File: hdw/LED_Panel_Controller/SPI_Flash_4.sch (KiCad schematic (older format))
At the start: 14 parts

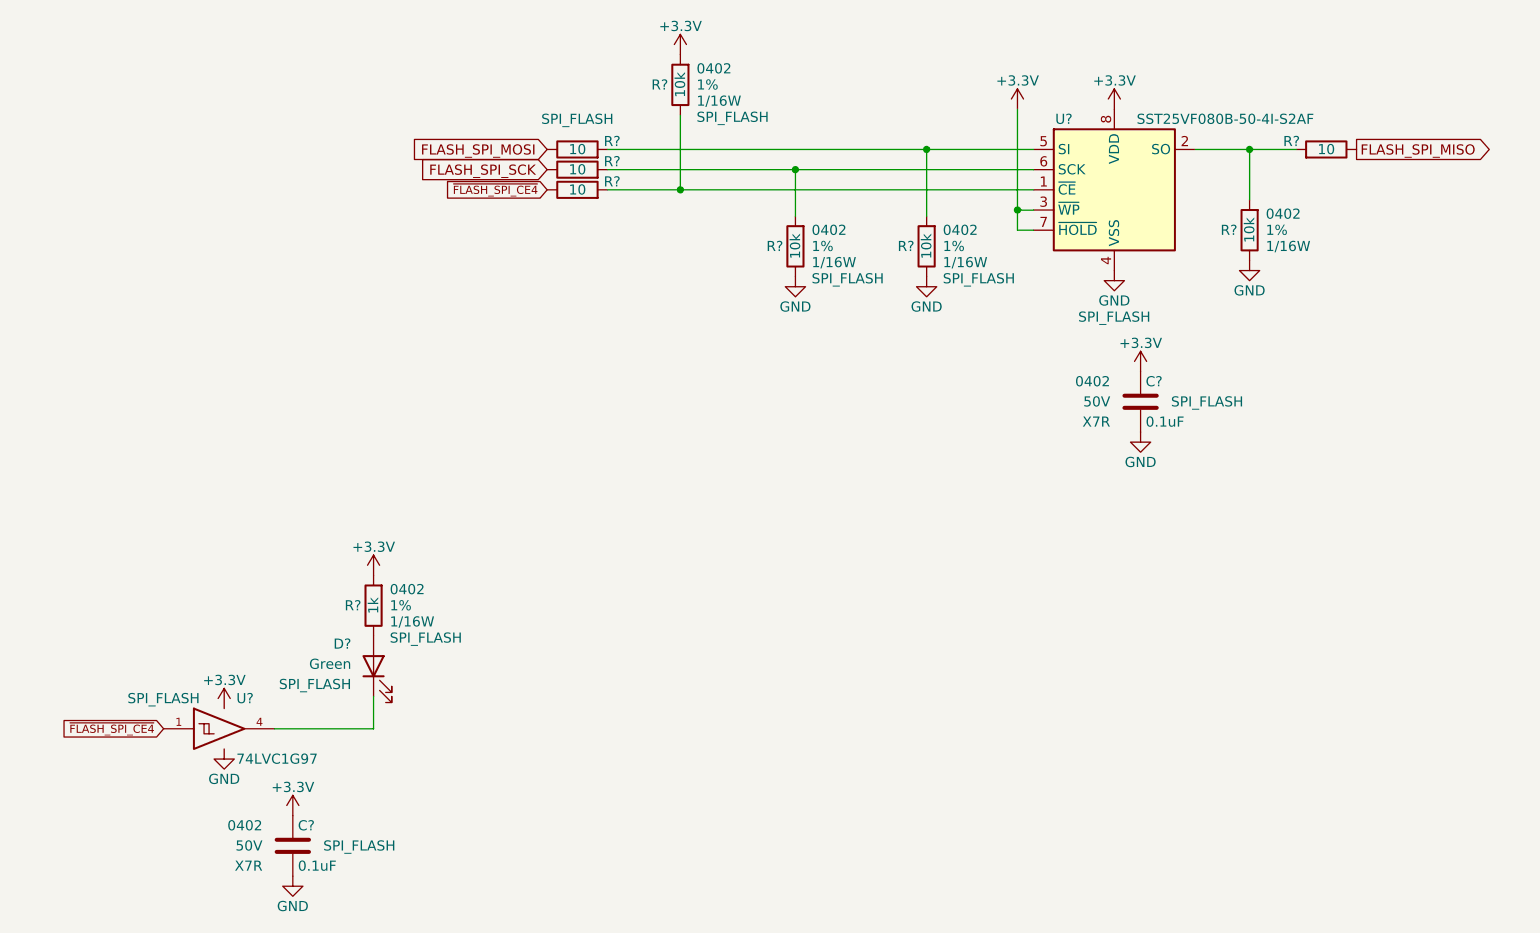
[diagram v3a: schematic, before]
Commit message: assigned I2C addresses
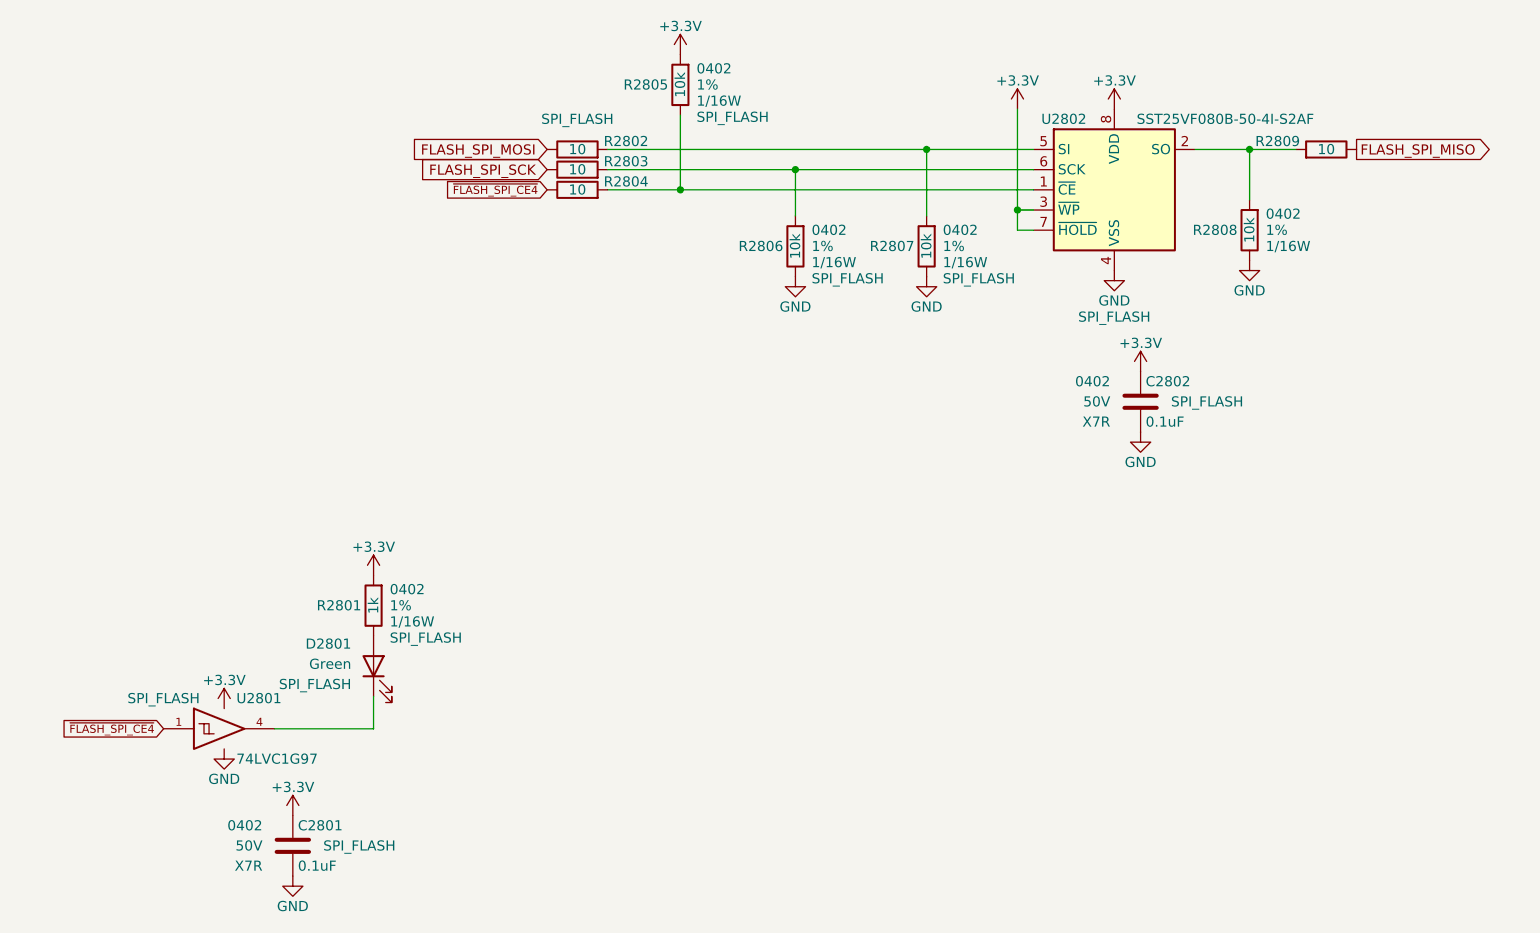
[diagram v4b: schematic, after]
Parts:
- removed C? (x2): 0.1uF, Capacitors_SMD:C_0402, symbol Custom_Library:C_Custom
- removed D?: Green, LEDs:LED_0402, symbol Device:LED
- removed R? (x4): 10k, Resistors_SMD:R_0402, symbol Custom_Library:R_Custom
- removed R? (x3): 10, Resistors_SMD:R_0402, symbol Custom_Library:R_Custom
- removed U?: SST25VF080B-50-4I-S2AF, Package_SO:SOIC-8_5.275x5.275mm_P1.27mm, symbol Memory_Flash:SST25VF080B-50-4x-S2Ax
- removed U?: 74LVC1G97, Package_TO_SOT_SMD:SOT-363_SC-70-6, symbol Custom_Library:74LVC1G97_Power_BUF
- added C2801, C2802: 0.1uF, Capacitors_SMD:C_0402, symbol Custom_Library:C_Custom
- added D2801: Green, LEDs:LED_0402, symbol Device:LED
- added R2802, R2803, R2809: 10, Resistors_SMD:R_0402, symbol Custom_Library:R_Custom
- added R2805, R2806, R2807, R2808: 10k, Resistors_SMD:R_0402, symbol Custom_Library:R_Custom
- added U2801: 74LVC1G97, Package_TO_SOT_SMD:SOT-363_SC-70-6, symbol Custom_Library:74LVC1G97_Power_BUF
- added U2802: SST25VF080B-50-4I-S2AF, Package_SO:SOIC-8_5.275x5.275mm_P1.27mm, symbol Memory_Flash:SST25VF080B-50-4x-S2Ax
- gave numbers to parts that had none: 2
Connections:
- net +3V3: now also C2801.1, C2802.1, R2805.1, U2801.5 (VCC), U2802.3 (~WP~), U2802.7 (~HOLD~), U2802.8 (VDD)
- net FLASH_SPI_MISO: now also R2809.2
- net FLASH_SPI_MOSI: now also R2802.2
- net FLASH_SPI_SCK: now also R2803.2
- net GND: now also C2801.2, C2802.2, R2806.2, R2807.2, R2808.2, U2801.2 (GND), U2801.3 (GND), U2801.6 (GND), U2802.4 (VSS)
- net ~FLASH_SPI_CE4: now also U2801.1
- net at R2801.2: now also D2801.2 (A)
- net at R2804.1: now also R2805.2, U2802.1 (~CE)
- new net: R2808.1, R2809.1, U2802.2 (SO)
- new net: R2802.1, R2807.1, U2802.5 (SI)
- new net: D2801.1 (K), U2801.4
- new net: R2803.1, R2806.1, U2802.6 (SCK)
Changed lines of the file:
@@
 $EndDescr
 $Comp
-L power:GND #PWR?
-U 1 1 5BB4E0E3
+L power:GND #PWR02811
+U 1 1 60786260
 P 6080 4050
-F 0 "#PWR?" H 6080 3800 50  0001 C CNN
+F 0 "#PWR02811" H 6080 3800 50  0001 C CNN
 F 1 "GND" H 6080 3900 50  0000 C CNN
 F 2 "" H 6080 4050 50  0001 C CNN
@@
 $EndComp
 $Comp
-L Custom_Library:R_Custom R?
-U 1 1 5BB4EDD1
+L Custom_Library:R_Custom R2808
+U 1 1 60786268
 P 6750 3850
-F 0 "R?" H 6690 3850 50  0000 R CNN
+F 0 "R2808" H 6690 3850 50  0000 R CNN
 F 1 "10k" V 6750 3850 50  0000 C CNN
 F 2 "Resistors_SMD:R_0402" H 6750 3850 50  0001 C CNN
@@
 $EndComp
 $Comp
-L power:GND #PWR?
-U 1 1 5BB4EE63
+L power:GND #PWR02808
+U 1 1 6078626E
 P 5150 4080
-F 0 "#PWR?" H 5150 3830 50  0001 C CNN
+F 0 "#PWR02808" H 5150 3830 50  0001 C CNN
 F 1 "GND" H 5150 3930 50  0000 C CNN
 F 2 "" H 5150 4080 50  0001 C CNN
@@
 $EndComp
 $Comp
-L power:GND #PWR?
-U 1 1 5BB4EE7C
+L power:GND #PWR02814
+U 1 1 60786273
 P 6750 4000
-F 0 "#PWR?" H 6750 3750 50  0001 C CNN
+F 0 "#PWR02814" H 6750 3750 50  0001 C CNN
 F 1 "GND" H 6750 3850 50  0000 C CNN
 F 2 "" H 6750 4000 50  0001 C CNN
@@
 $EndComp
 $Comp
-L Custom_Library:R_Custom R?
-U 1 1 5BB4F53B
+L Custom_Library:R_Custom R2802
+U 1 1 60786279
 P 3420 3450
-F 0 "R?" V 3380 3580 50  0000 L CNN
+F 0 "R2802" V 3380 3580 50  0000 L CNN
 F 1 "10" V 3420 3450 50  0000 C CNN
 F 2 "Resistors_SMD:R_0402" H 3420 3450 50  0001 C CNN
@@
 	3570 3650 3930 3650
 $Comp
-L power:+3.3V #PWR?
-U 1 1 5BDF3D33
+L power:+3.3V #PWR02806
+U 1 1 60786284
 P 3930 2980
-F 0 "#PWR?" H 3930 2830 50  0001 C CNN
+F 0 "#PWR02806" H 3930 2830 50  0001 C CNN
 F 1 "+3.3V" H 3930 3120 50  0000 C CNN
 F 2 "" H 3930 2980 50  0001 C CNN
@@
 $EndComp
 $Comp
-L power:+3.3V #PWR?
-U 1 1 5BDF3DF4
+L power:+3.3V #PWR02810
+U 1 1 60786289
 P 6080 3250
-F 0 "#PWR?" H 6080 3100 50  0001 C CNN
+F 0 "#PWR02810" H 6080 3100 50  0001 C CNN
 F 1 "+3.3V" H 6080 3390 50  0000 C CNN
 F 2 "" H 6080 3250 50  0001 C CNN
@@
 $Comp
 L Custom_Library:C_Custom C?
-U 1 1 5C15F697
+U 1 1 60786291
 P 2010 6900
-AR Path="/5BAAE16C/5C15F697" Ref="C?"  Part="1"
-AR Path="/5BB181D8/5C15F697" Ref="C?"  Part="1"
-AR Path="/5BB2595E/5C15F697" Ref="C?"  Part="1"
-AR Path="/5F583577/5C15F697" Ref="C?"  Part="1"
-AR Path="/5F58359E/5C15F697" Ref="C?"  Part="1"
-F 0 "C?" H 2035 7000 50  0000 L CNN
+AR Path="/5BAAE16C/60786291" Ref="C?"  Part="1"
+AR Path="/5BB181D8/60786291" Ref="C?"  Part="1"
+AR Path="/5BB2595E/60786291" Ref="C?"  Part="1"
+AR Path="/5F583577/60786291" Ref="C?"  Part="1"
+AR Path="/5F58359E/60786291" Ref="C2801"  Part="1"
+F 0 "C2801" H 2035 7000 50  0000 L CNN
 F 1 "0.1uF" H 2035 6800 50  0000 L CNN
 F 2 "Capacitors_SMD:C_0402" H 2048 6750 50  0001 C CNN
@@
 $EndComp
 $Comp
-L power:+3.3V #PWR?
-U 1 1 5C161B83
+L power:+3.3V #PWR02801
+U 1 1 60786298
 P 1670 6220
-F 0 "#PWR?" H 1670 6070 50  0001 C CNN
+F 0 "#PWR02801" H 1670 6070 50  0001 C CNN
 F 1 "+3.3V" H 1670 6360 50  0000 C CNN
 F 2 "" H 1670 6220 50  0001 C CNN
@@
 $EndComp
 $Comp
-L power:+3.3V #PWR?
-U 1 1 5C161BE9
+L power:+3.3V #PWR02803
+U 1 1 6078629D
 P 2010 6750
-F 0 "#PWR?" H 2010 6600 50  0001 C CNN
+F 0 "#PWR02803" H 2010 6600 50  0001 C CNN
 F 1 "+3.3V" H 2010 6890 50  0000 C CNN
 F 2 "" H 2010 6750 50  0001 C CNN
@@
 $EndComp
 $Comp
-L power:GND #PWR?
+L power:GND #PWR02804
 U 1 1 5C161C44
 P 2010 7050
-F 0 "#PWR?" H 2010 6800 50  0001 C CNN
+F 0 "#PWR02804" H 2010 6800 50  0001 C CNN
 F 1 "GND" H 2010 6900 50  0000 C CNN
 F 2 "" H 2010 7050 50  0001 C CNN
@@
 $EndComp
 $Comp
-L power:GND #PWR?
-U 1 1 5C161C9F
+L power:GND #PWR02802
+U 1 1 607862AF
 P 1670 6420
-F 0 "#PWR?" H 1670 6170 50  0001 C CNN
+F 0 "#PWR02802" H 1670 6170 50  0001 C CNN
 F 1 "GND" H 1670 6270 50  0000 C CNN
 F 2 "" H 1670 6420 50  0001 C CNN
@@
 $Comp
 L power:+3.3V #PWR?
-U 1 1 5C166A81
+U 1 1 607862B1
 P 2410 5560
-AR Path="/5BB844FD/5C166A81" Ref="#PWR?"  Part="1"
-AR Path="/5BF346B3/5C166A81" Ref="#PWR?"  Part="1"
-AR Path="/5BB2595E/5C166A81" Ref="#PWR?"  Part="1"
-AR Path="/5F583577/5C166A81" Ref="#PWR?"  Part="1"
-AR Path="/5F58359E/5C166A81" Ref="#PWR?"  Part="1"
-F 0 "#PWR?" H 2410 5410 50  0001 C CNN
+AR Path="/5BB844FD/607862B1" Ref="#PWR?"  Part="1"
+AR Path="/5BF346B3/607862B1" Ref="#PWR?"  Part="1"
+AR Path="/5BB2595E/607862B1" Ref="#PWR?"  Part="1"
+AR Path="/5F583577/607862B1" Ref="#PWR?"  Part="1"
+AR Path="/5F58359E/607862B1" Ref="#PWR02805"  Part="1"
+F 0 "#PWR02805" H 2410 5410 50  0001 C CNN
 F 1 "+3.3V" H 2410 5700 50  0000 C CNN
 F 2 "" H 2410 5560 50  0001 C CNN
@@
 $Comp
 L Device:LED D?
-U 1 1 5C166A95
+U 1 1 607862BA
 P 2410 6010
-AR Path="/5BB844FD/5C166A95" Ref="D?"  Part="1"
-AR Path="/5BF346B3/5C166A95" Ref="D?"  Part="1"
-AR Path="/5BB2595E/5C166A95" Ref="D?"  Part="1"
-AR Path="/5F583577/5C166A95" Ref="D?"  Part="1"
-AR Path="/5F58359E/5C166A95" Ref="D?"  Part="1"
-F 0 "D?" V 2520 6120 50  0000 L CNN
+AR Path="/5BB844FD/607862BA" Ref="D?"  Part="1"
+AR Path="/5BF346B3/607862BA" Ref="D?"  Part="1"
+AR Path="/5BB2595E/607862BA" Ref="D?"  Part="1"
+AR Path="/5F583577/607862BA" Ref="D?"  Part="1"
+AR Path="/5F58359E/607862BA" Ref="D2801"  Part="1"
+F 0 "D2801" V 2520 6120 50  0000 L CNN
 F 1 "Green" V 2420 6120 50  0000 L CNN
 F 2 "LEDs:LED_0402" H 2410 6010 50  0001 C CNN
@@
 $EndComp
 $Comp
-L Memory_Flash:SST25VF080B-50-4x-S2Ax U?
-U 1 1 5F6879D5
+L Memory_Flash:SST25VF080B-50-4x-S2Ax U2802
+U 1 1 607862F8
 P 6080 3650
-F 0 "U?" H 5830 4000 50  0000 C CNN
+F 0 "U2802" H 5830 4000 50  0000 C CNN
 F 1 "SST25VF080B-50-4I-S2AF" H 6630 4000 50  0000 C CNN
 F 2 "Package_SO:SOIC-8_5.275x5.275mm_P1.27mm" H 6080 2950 50  0001 C CNN
@@
 $EndComp
 $Comp
-L power:+3.3V #PWR?
-U 1 1 5F689292
+L power:+3.3V #PWR02812
+U 1 1 607862FF
 P 6210 4550
-F 0 "#PWR?" H 6210 4400 50  0001 C CNN
+F 0 "#PWR02812" H 6210 4400 50  0001 C CNN
 F 1 "+3.3V" H 6210 4690 50  0000 C CNN
 F 2 "" H 6210 4550 50  0001 C CNN
@@
 $EndComp
 $Comp
-L power:GND #PWR?
-U 1 1 5F689298
+L power:GND #PWR02813
+U 1 1 60786305
 P 6210 4850
-F 0 "#PWR?" H 6210 4600 50  0001 C CNN
+F 0 "#PWR02813" H 6210 4600 50  0001 C CNN
 F 1 "GND" H 6210 4700 50  0000 C CNN
 F 2 "" H 6210 4850 50  0001 C CNN
@@
 $EndComp
 $Comp
-L power:+3.3V #PWR?
-U 1 1 5F69329F
+L power:+3.3V #PWR02809
+U 1 1 6078630B
 P 5600 3250
-F 0 "#PWR?" H 5600 3100 50  0001 C CNN
+F 0 "#PWR02809" H 5600 3100 50  0001 C CNN
 F 1 "+3.3V" H 5600 3390 50  0000 C CNN
 F 2 "" H 5600 3250 50  0001 C CNN
@@
 	3570 3550 4500 3550
 $Comp
-L Custom_Library:R_Custom R?
-U 1 1 5F697048
+L Custom_Library:R_Custom R2806
+U 1 1 60786318
 P 4500 3930
-F 0 "R?" H 4440 3930 50  0000 R CNN
+F 0 "R2806" H 4440 3930 50  0000 R CNN
 F 1 "10k" V 4500 3930 50  0000 C CNN
 F 2 "Resistors_SMD:R_0402" H 4500 3930 50  0001 C CNN
@@
 $EndComp
 $Comp
-L power:GND #PWR?
-U 1 1 5F697052
+L power:GND #PWR02807
+U 1 1 6078631D
 P 4500 4080
-F 0 "#PWR?" H 4500 3830 50  0001 C CNN
+F 0 "#PWR02807" H 4500 3830 50  0001 C CNN
 F 1 "GND" H 4500 3930 50  0000 C CNN
 F 2 "" H 4500 4080 50  0001 C CNN
@@
 	4500 3550 5680 3550
 $Comp
-L Custom_Library:R_Custom R?
-U 1 1 5F7379BB
+L Custom_Library:R_Custom R2803
+U 1 1 60786325
 P 3420 3550
-F 0 "R?" V 3380 3680 50  0000 L CNN
+F 0 "R2803" V 3380 3680 50  0000 L CNN
 F 1 "10" V 3420 3550 50  0000 C CNN
 F 2 "Resistors_SMD:R_0402" H 3420 3550 50  0001 C CNN
@@
 $EndComp
 $Comp
-L Custom_Library:R_Custom R?
+L Custom_Library:R_Custom R2804
 U 1 1 5F737B74
 P 3420 3650
-F 0 "R?" V 3380 3780 50  0000 L CNN
+F 0 "R2804" V 3380 3780 50  0000 L CNN
 F 1 "10" V 3420 3650 50  0000 C CNN
 F 2 "Resistors_SMD:R_0402" H 3420 3650 50  0001 C CNN
@@
 $EndComp
 $Comp
-L Custom_Library:R_Custom R?
-U 1 1 5F737D15
+L Custom_Library:R_Custom R2809
+U 1 1 6078632F
 P 7130 3450
-F 0 "R?" V 7090 3580 50  0000 L CNN
+F 0 "R2809" V 7090 3580 50  0000 L CNN
 F 1 "10" V 7130 3450 50  0000 C CNN
 F 2 "Resistors_SMD:R_0402" H 7130 3450 50  0001 C CNN
@@
 $EndComp
 $Comp
-L Custom_Library:74LVC1G97_Power_BUF U?
-U 1 1 5FE9D8D5
+L Custom_Library:74LVC1G97_Power_BUF U2801
+U 1 1 60786347
 P 1670 6320
-F 0 "U?" H 1730 6470 50  0000 L CNN
+F 0 "U2801" H 1730 6470 50  0000 L CNN
 F 1 "74LVC1G97" H 1730 6170 50  0000 L CNN
 F 2 "Package_TO_SOT_SMD:SOT-363_SC-70-6" H 1720 6320 50  0001 C CNN
@@
 $EndComp
 $Comp
-L Custom_Library:R_Custom R?
-U 1 1 6026393A
+L Custom_Library:R_Custom R2807
+U 1 1 60786358
 P 5150 3930
-F 0 "R?" H 5090 3930 50  0000 R CNN
+F 0 "R2807" H 5090 3930 50  0000 R CNN
 F 1 "10k" V 5150 3930 50  0000 C CNN
 F 2 "Resistors_SMD:R_0402" H 5150 3930 50  0001 C CNN
@@
 $EndComp
 $Comp
-L Custom_Library:R_Custom R?
-U 1 1 60263FB7
+L Custom_Library:R_Custom R2805
+U 1 1 6078635C
 P 3930 3130
-F 0 "R?" H 3870 3130 50  0000 R CNN
+F 0 "R2805" H 3870 3130 50  0000 R CNN
 F 1 "10k" V 3930 3130 50  0000 C CNN
 F 2 "Resistors_SMD:R_0402" H 3930 3130 50  0001 C CNN
@@
 $EndComp
 $Comp
-L Custom_Library:R_Custom R?
+L Custom_Library:R_Custom R2801
 U 1 1 60266213
 P 2410 5710
-F 0 "R?" H 2350 5710 50  0000 R CNN
+F 0 "R2801" H 2350 5710 50  0000 R CNN
 F 1 "1k" V 2410 5710 50  0000 C CNN
 F 2 "Resistors_SMD:R_0402" H 2410 5710 50  0001 C CNN
@@
 $Comp
 L Custom_Library:C_Custom C?
-U 1 1 60269564
+U 1 1 6078636D
 P 6210 4700
-AR Path="/5BAAE16C/60269564" Ref="C?"  Part="1"
-AR Path="/5BB181D8/60269564" Ref="C?"  Part="1"
-AR Path="/5BB2595E/60269564" Ref="C?"  Part="1"
-AR Path="/5F583577/60269564" Ref="C?"  Part="1"
-AR Path="/5F58359E/60269564" Ref="C?"  Part="1"
-F 0 "C?" H 6235 4800 50  0000 L CNN
+AR Path="/5BAAE16C/6078636D" Ref="C?"  Part="1"
+AR Path="/5BB181D8/6078636D" Ref="C?"  Part="1"
+AR Path="/5BB2595E/6078636D" Ref="C?"  Part="1"
+AR Path="/5F583577/6078636D" Ref="C?"  Part="1"
+AR Path="/5F58359E/6078636D" Ref="C2802"  Part="1"
+F 0 "C2802" H 6235 4800 50  0000 L CNN
 F 1 "0.1uF" H 6235 4600 50  0000 L CNN
 F 2 "Capacitors_SMD:C_0402" H 6248 4550 50  0001 C CNN
